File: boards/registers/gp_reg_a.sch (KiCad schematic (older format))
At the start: 28 parts

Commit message: Annotated schematics, assigned footprints
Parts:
- C28, C29: renamed from C?; footprint (none) -> Capacitor_SMD:C_0805_2012Metric
- D54, D55, D56, D57, D58, D59, D60, D61: renamed from D?; footprint (none) -> LED_SMD:LED_0805_2012Metric
- R150, R151, R152, R153, R154, R155, R156, R157, R158, R159, R160, R161, R162, R163, R164, R165: renamed from R?; footprint (none) -> Resistor_SMD:R_0805_2012Metric
- U28: renamed from U?; footprint (none) -> Package_SO:SOIC-20W_7.5x12.8mm_P1.27mm
- U29: renamed from U?; footprint (none) -> Package_SO:SO-20_12.8x7.5mm_P1.27mm

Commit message: PCB attempt
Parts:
- U28: footprint Package_SO:SOIC-20W_7.5x12.8mm_P1.27mm -> Package_SO:TSSOP-20_4.4x6.5mm_P0.65mm
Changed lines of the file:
@@
 AR Path="/5E7CA397/5EA6BD49" Ref="U?"  Part="1"
 AR Path="/5E9FD18D/5EA6BD49" Ref="U29"  Part="1"
-F 0 "U29" H 7600 1150 50  0000 C CNN
+F 0 "U29" H 7650 1150 50  0000 C CNN
 F 1 "74ACT244" H 7550 1050 50  0000 C CNN
 F 2 "Package_SO:SO-20_12.8x7.5mm_P1.27mm" H 7250 1700 50  0001 C CNN
@@
 AR Path="/5E7CA397/5EA6BDD0" Ref="U?"  Part="1"
 AR Path="/5E9FD18D/5EA6BDD0" Ref="U28"  Part="1"
-F 0 "U28" H 5100 1150 50  0000 C CNN
+F 0 "U28" H 5150 1150 50  0000 C CNN
 F 1 "74AC273" H 5100 1050 50  0000 C CNN
-F 2 "Package_SO:SOIC-20W_7.5x12.8mm_P1.27mm" H 4750 1700 50  0001 C CNN
+F 2 "Package_SO:TSSOP-20_4.4x6.5mm_P0.65mm" H 4750 1700 50  0001 C CNN
 F 3 "https://assets.nexperia.com/documents/data-sheet/74HC_HCT273.pdf" H 4750 1700 50  0001 C CNN
 	1    4750 1700

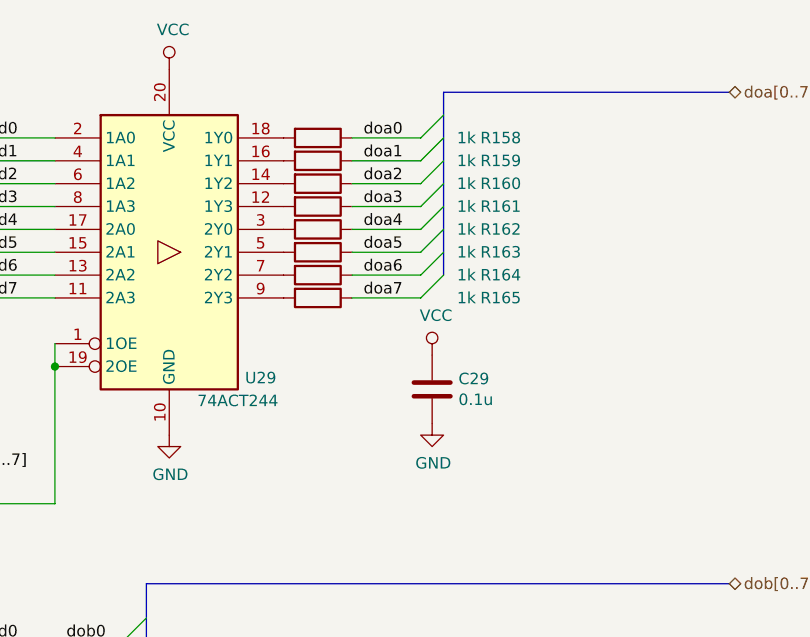
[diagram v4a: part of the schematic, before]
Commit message: CPU registers board
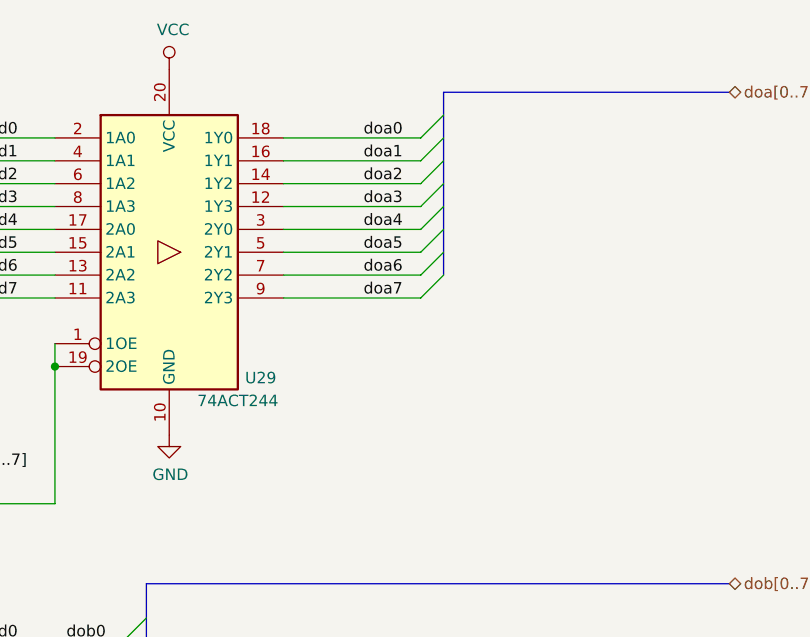
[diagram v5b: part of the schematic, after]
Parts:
- removed C29: 0.1u, Capacitor_SMD:C_0805_2012Metric, symbol Device:C
- removed R158, R159, R160, R161, R162, R163, R164, R165: 1k, Resistor_SMD:R_0805_2012Metric, symbol Device:R
- U29: footprint Package_SO:SO-20_12.8x7.5mm_P1.27mm -> Package_SO:TSSOP-20_4.4x6.5mm_P0.65mm
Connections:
- net doa0: now also U29.18 (1Y0)
- net doa1: now also U29.16 (1Y1)
- net doa2: now also U29.14 (1Y2)
- net doa3: now also U29.12 (1Y3)
- net doa4: now also U29.3 (2Y0)
- net doa5: now also U29.5 (2Y1)
- net doa6: now also U29.7 (2Y2)
- net doa7: now also U29.9 (2Y3)
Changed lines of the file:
@@
 F 0 "U29" H 7650 1150 50  0000 C CNN
 F 1 "74ACT244" H 7550 1050 50  0000 C CNN
-F 2 "Package_SO:SO-20_12.8x7.5mm_P1.27mm" H 7250 1700 50  0001 C CNN
+F 2 "Package_SO:TSSOP-20_4.4x6.5mm_P0.65mm" H 7250 1700 50  0001 C CNN
 F 3 "https://assets.nexperia.com/documents/data-sheet/74HC_HCT244.pdf" H 7250 1700 50  0001 C CNN
 	1    7250 1700
@@
 Entry Wire Line
 	8350 1900 8450 1800
-Wire Wire Line
-	8350 1200 8050 1200
-Wire Wire Line
-	8050 1300 8350 1300
-Wire Wire Line
-	8350 1400 8050 1400
-Wire Wire Line
-	8050 1500 8350 1500
-Wire Wire Line
-	8350 1600 8050 1600
-Wire Wire Line
-	8050 1700 8350 1700
-Wire Wire Line
-	8350 1800 8050 1800
-Wire Wire Line
-	8050 1900 8350 1900
 Text Label 6500 1200 0    50   ~ 0
 d0
@@
 $Comp
 L Device:C C?
-U 1 1 5EA6BED9
-P 8400 2300
-AR Path="/5E73B7F6/5EA6BED9" Ref="C?"  Part="1"
-AR Path="/5E7CA397/5EA6BED9" Ref="C?"  Part="1"
-AR Path="/5E9FD18D/5EA6BED9" Ref="C29"  Part="1"
-F 0 "C29" H 8515 2346 50  0000 L CNN
-F 1 "0.1u" H 8515 2255 50  0000 L CNN
-F 2 "Capacitor_SMD:C_0805_2012Metric" H 8438 2150 50  0001 C CNN
-F 3 "~" H 8400 2300 50  0001 C CNN
-	1    8400 2300
-	1    0    0    -1
-$EndComp
-$Comp
-L power:GND #PWR?
-U 1 1 5EA6BEDF
-P 8400 2450
-AR Path="/5E73B7F6/5EA6BEDF" Ref="#PWR?"  Part="1"
-AR Path="/5E7CA397/5EA6BEDF" Ref="#PWR?"  Part="1"
-AR Path="/5E9FD18D/5EA6BEDF" Ref="#PWR0189"  Part="1"
-F 0 "#PWR0189" H 8400 2200 50  0001 C CNN
-F 1 "GND" H 8405 2277 50  0000 C CNN
-F 2 "" H 8400 2450 50  0001 C CNN
-F 3 "" H 8400 2450 50  0001 C CNN
-	1    8400 2450
-	1    0    0    -1
-$EndComp
-$Comp
-L power:VCC #PWR?
-U 1 1 5EA6BEE5
-P 8400 2150
-AR Path="/5E73B7F6/5EA6BEE5" Ref="#PWR?"  Part="1"
-AR Path="/5E7CA397/5EA6BEE5" Ref="#PWR?"  Part="1"
-AR Path="/5E9FD18D/5EA6BEE5" Ref="#PWR0188"  Part="1"
-F 0 "#PWR0188" H 8400 2000 50  0001 C CNN
-F 1 "VCC" H 8417 2323 50  0000 C CNN
-F 2 "" H 8400 2150 50  0001 C CNN
-F 3 "" H 8400 2150 50  0001 C CNN
-	1    8400 2150
-	1    0    0    -1
-$EndComp
-$Comp
-L Device:C C?
 U 1 1 5EA6BEEB
 P 4050 2400
@@
 	0    1    1    0
 $EndComp
-$Comp
-L Device:R R?
-U 1 1 5EA6BEFD
-P 7900 1200
-AR Path="/5E7CA397/5EA6BEFD" Ref="R?"  Part="1"
-AR Path="/5E73B7F6/5EA6BEFD" Ref="R?"  Part="1"
-AR Path="/5E9FD18D/5EA6BEFD" Ref="R158"  Part="1"
-F 0 "R158" V 7900 2000 50  0000 C CNN
-F 1 "1k" V 7900 1850 50  0000 C CNN
-F 2 "Resistor_SMD:R_0805_2012Metric" V 7830 1200 50  0001 C CNN
-F 3 "~" H 7900 1200 50  0001 C CNN
-	1    7900 1200
-	0    1    1    0
-$EndComp
-$Comp
-L Device:R R?
-U 1 1 5EA6BF03
-P 7900 1300
-AR Path="/5E7CA397/5EA6BF03" Ref="R?"  Part="1"
-AR Path="/5E73B7F6/5EA6BF03" Ref="R?"  Part="1"
-AR Path="/5E9FD18D/5EA6BF03" Ref="R159"  Part="1"
-F 0 "R159" V 7900 2100 50  0000 C CNN
-F 1 "1k" V 7900 1950 50  0000 C CNN
-F 2 "Resistor_SMD:R_0805_2012Metric" V 7830 1300 50  0001 C CNN
-F 3 "~" H 7900 1300 50  0001 C CNN
-	1    7900 1300
-	0    1    1    0
-$EndComp
-$Comp
-L Device:R R?
-U 1 1 5EA6BF09
-P 7900 1400
-AR Path="/5E7CA397/5EA6BF09" Ref="R?"  Part="1"
-AR Path="/5E73B7F6/5EA6BF09" Ref="R?"  Part="1"
-AR Path="/5E9FD18D/5EA6BF09" Ref="R160"  Part="1"
-F 0 "R160" V 7900 2200 50  0000 C CNN
-F 1 "1k" V 7900 2050 50  0000 C CNN
-F 2 "Resistor_SMD:R_0805_2012Metric" V 7830 1400 50  0001 C CNN
-F 3 "~" H 7900 1400 50  0001 C CNN
-	1    7900 1400
-	0    1    1    0
-$EndComp
-$Comp
-L Device:R R?
-U 1 1 5EA6BF0F
-P 7900 1500
-AR Path="/5E7CA397/5EA6BF0F" Ref="R?"  Part="1"
-AR Path="/5E73B7F6/5EA6BF0F" Ref="R?"  Part="1"
-AR Path="/5E9FD18D/5EA6BF0F" Ref="R161"  Part="1"
-F 0 "R161" V 7900 2300 50  0000 C CNN
-F 1 "1k" V 7900 2150 50  0000 C CNN
-F 2 "Resistor_SMD:R_0805_2012Metric" V 7830 1500 50  0001 C CNN
-F 3 "~" H 7900 1500 50  0001 C CNN
-	1    7900 1500
-	0    1    1    0
-$EndComp
-$Comp
-L Device:R R?
-U 1 1 5EA6BF15
-P 7900 1600
-AR Path="/5E7CA397/5EA6BF15" Ref="R?"  Part="1"
-AR Path="/5E73B7F6/5EA6BF15" Ref="R?"  Part="1"
-AR Path="/5E9FD18D/5EA6BF15" Ref="R162"  Part="1"
-F 0 "R162" V 7900 2400 50  0000 C CNN
-F 1 "1k" V 7900 2250 50  0000 C CNN
-F 2 "Resistor_SMD:R_0805_2012Metric" V 7830 1600 50  0001 C CNN
-F 3 "~" H 7900 1600 50  0001 C CNN
-	1    7900 1600
-	0    1    1    0
-$EndComp
-$Comp
-L Device:R R?
-U 1 1 5EA6BF1B
-P 7900 1700
-AR Path="/5E7CA397/5EA6BF1B" Ref="R?"  Part="1"
-AR Path="/5E73B7F6/5EA6BF1B" Ref="R?"  Part="1"
-AR Path="/5E9FD18D/5EA6BF1B" Ref="R163"  Part="1"
-F 0 "R163" V 7900 2500 50  0000 C CNN
-F 1 "1k" V 7900 2350 50  0000 C CNN
-F 2 "Resistor_SMD:R_0805_2012Metric" V 7830 1700 50  0001 C CNN
-F 3 "~" H 7900 1700 50  0001 C CNN
-	1    7900 1700
-	0    1    1    0
-$EndComp
-$Comp
-L Device:R R?
-U 1 1 5EA6BF21
-P 7900 1800
-AR Path="/5E7CA397/5EA6BF21" Ref="R?"  Part="1"
-AR Path="/5E73B7F6/5EA6BF21" Ref="R?"  Part="1"
-AR Path="/5E9FD18D/5EA6BF21" Ref="R164"  Part="1"
-F 0 "R164" V 7900 2600 50  0000 C CNN
-F 1 "1k" V 7900 2450 50  0000 C CNN
-F 2 "Resistor_SMD:R_0805_2012Metric" V 7830 1800 50  0001 C CNN
-F 3 "~" H 7900 1800 50  0001 C CNN
-	1    7900 1800
-	0    1    1    0
-$EndComp
-$Comp
-L Device:R R?
-U 1 1 5EA6BF27
-P 7900 1900
-AR Path="/5E7CA397/5EA6BF27" Ref="R?"  Part="1"
-AR Path="/5E73B7F6/5EA6BF27" Ref="R?"  Part="1"
-AR Path="/5E9FD18D/5EA6BF27" Ref="R165"  Part="1"
-F 0 "R165" V 7900 2700 50  0000 C CNN
-F 1 "1k" V 7900 2550 50  0000 C CNN
-F 2 "Resistor_SMD:R_0805_2012Metric" V 7830 1900 50  0001 C CNN
-F 3 "~" H 7900 1900 50  0001 C CNN
-	1    7900 1900
-	0    1    1    0
-$EndComp
 Text HLabel 1650 2800 0    50   Input ~ 0
 ~oea
@@
 Wire Bus Line
 	9700 3150 7150 3150
+Wire Wire Line
+	7750 1900 8350 1900
+Wire Wire Line
+	7750 1800 8350 1800
+Wire Wire Line
+	7750 1700 8350 1700
+Wire Wire Line
+	7750 1600 8350 1600
+Wire Wire Line
+	7750 1500 8350 1500
+Wire Wire Line
+	7750 1400 8350 1400
+Wire Wire Line
+	7750 1300 8350 1300
+Wire Wire Line
+	7750 1200 8350 1200
 Wire Bus Line
 	7150 3150 7150 4000

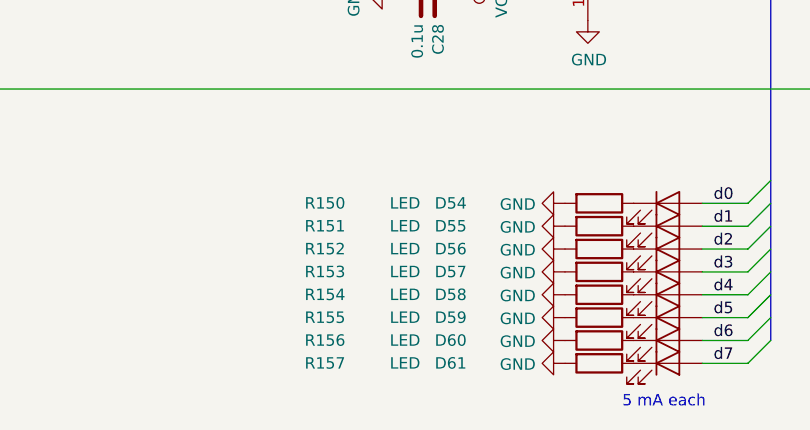
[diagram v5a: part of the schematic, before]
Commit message: LEDs and LED resistors
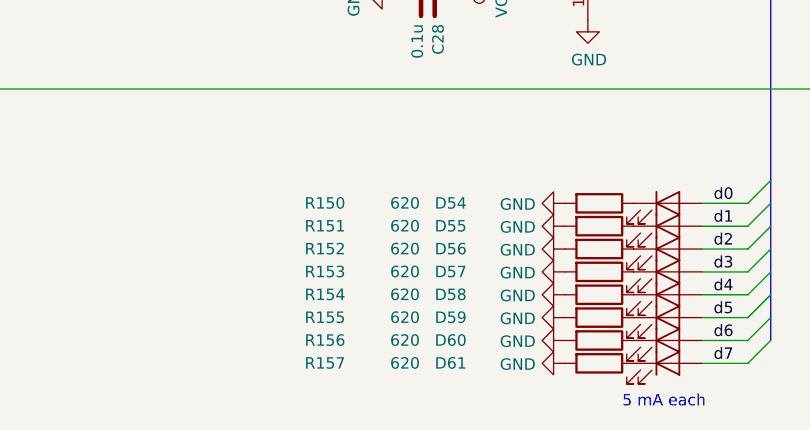
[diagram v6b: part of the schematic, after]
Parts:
- D54, D55, D56, D57, D58, D59, D60, D61: value LED -> KP-2012EC
- R150, R151, R152, R153, R154, R155, R156, R157: value LED -> 620
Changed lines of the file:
@@
 AR Path="/5E9FD18D/5EA6BE13" Ref="D54"  Part="1"
 F 0 "D54" H 4150 3300 50  0000 C CNN
-F 1 "LED" H 5093 3425 50  0001 C CNN
+F 1 "KP-2012EC" H 5093 3425 50  0001 C CNN
 F 2 "LED_SMD:LED_0805_2012Metric" H 5100 3300 50  0001 C CNN
 F 3 "~" H 5100 3300 50  0001 C CNN
@@
 AR Path="/5E9FD18D/5EA6BE19" Ref="R150"  Part="1"
 F 0 "R150" V 4800 2100 50  0000 C CNN
-F 1 "LED" V 4800 2450 50  0000 C CNN
+F 1 "620" V 4800 2450 50  0000 C CNN
 F 2 "Resistor_SMD:R_0805_2012Metric" V 4730 3300 50  0001 C CNN
 F 3 "~" H 4800 3300 50  0001 C CNN
@@
 AR Path="/5E9FD18D/5EA6BE25" Ref="D55"  Part="1"
 F 0 "D55" H 4150 3400 50  0000 C CNN
-F 1 "LED" H 5093 3525 50  0001 C CNN
+F 1 "KP-2012EC" H 5093 3525 50  0001 C CNN
 F 2 "LED_SMD:LED_0805_2012Metric" H 5100 3400 50  0001 C CNN
 F 3 "~" H 5100 3400 50  0001 C CNN
@@
 AR Path="/5E9FD18D/5EA6BE2B" Ref="R151"  Part="1"
 F 0 "R151" V 4800 2200 50  0000 C CNN
-F 1 "LED" V 4800 2550 50  0000 C CNN
+F 1 "620" V 4800 2550 50  0000 C CNN
 F 2 "Resistor_SMD:R_0805_2012Metric" V 4730 3400 50  0001 C CNN
 F 3 "~" H 4800 3400 50  0001 C CNN
@@
 AR Path="/5E9FD18D/5EA6BE37" Ref="D56"  Part="1"
 F 0 "D56" H 4150 3500 50  0000 C CNN
-F 1 "LED" H 5093 3625 50  0001 C CNN
+F 1 "KP-2012EC" H 5093 3625 50  0001 C CNN
 F 2 "LED_SMD:LED_0805_2012Metric" H 5100 3500 50  0001 C CNN
 F 3 "~" H 5100 3500 50  0001 C CNN
@@
 AR Path="/5E9FD18D/5EA6BE3D" Ref="R152"  Part="1"
 F 0 "R152" V 4800 2300 50  0000 C CNN
-F 1 "LED" V 4800 2650 50  0000 C CNN
+F 1 "620" V 4800 2650 50  0000 C CNN
 F 2 "Resistor_SMD:R_0805_2012Metric" V 4730 3500 50  0001 C CNN
 F 3 "~" H 4800 3500 50  0001 C CNN
@@
 AR Path="/5E9FD18D/5EA6BE49" Ref="D57"  Part="1"
 F 0 "D57" H 4150 3600 50  0000 C CNN
-F 1 "LED" H 5093 3725 50  0001 C CNN
+F 1 "KP-2012EC" H 5093 3725 50  0001 C CNN
 F 2 "LED_SMD:LED_0805_2012Metric" H 5100 3600 50  0001 C CNN
 F 3 "~" H 5100 3600 50  0001 C CNN
@@
 AR Path="/5E9FD18D/5EA6BE4F" Ref="R153"  Part="1"
 F 0 "R153" V 4800 2400 50  0000 C CNN
-F 1 "LED" V 4800 2750 50  0000 C CNN
+F 1 "620" V 4800 2750 50  0000 C CNN
 F 2 "Resistor_SMD:R_0805_2012Metric" V 4730 3600 50  0001 C CNN
 F 3 "~" H 4800 3600 50  0001 C CNN
@@
 AR Path="/5E9FD18D/5EA6BE5B" Ref="D58"  Part="1"
 F 0 "D58" H 4150 3700 50  0000 C CNN
-F 1 "LED" H 5093 3825 50  0001 C CNN
+F 1 "KP-2012EC" H 5093 3825 50  0001 C CNN
 F 2 "LED_SMD:LED_0805_2012Metric" H 5100 3700 50  0001 C CNN
 F 3 "~" H 5100 3700 50  0001 C CNN
@@
 AR Path="/5E9FD18D/5EA6BE61" Ref="R154"  Part="1"
 F 0 "R154" V 4800 2500 50  0000 C CNN
-F 1 "LED" V 4800 2850 50  0000 C CNN
+F 1 "620" V 4800 2850 50  0000 C CNN
 F 2 "Resistor_SMD:R_0805_2012Metric" V 4730 3700 50  0001 C CNN
 F 3 "~" H 4800 3700 50  0001 C CNN
@@
 AR Path="/5E9FD18D/5EA6BE6D" Ref="D59"  Part="1"
 F 0 "D59" H 4150 3800 50  0000 C CNN
-F 1 "LED" H 5093 3925 50  0001 C CNN
+F 1 "KP-2012EC" H 5093 3925 50  0001 C CNN
 F 2 "LED_SMD:LED_0805_2012Metric" H 5100 3800 50  0001 C CNN
 F 3 "~" H 5100 3800 50  0001 C CNN
@@
 AR Path="/5E9FD18D/5EA6BE73" Ref="R155"  Part="1"
 F 0 "R155" V 4800 2600 50  0000 C CNN
-F 1 "LED" V 4800 2950 50  0000 C CNN
+F 1 "620" V 4800 2950 50  0000 C CNN
 F 2 "Resistor_SMD:R_0805_2012Metric" V 4730 3800 50  0001 C CNN
 F 3 "~" H 4800 3800 50  0001 C CNN
@@
 AR Path="/5E9FD18D/5EA6BE7F" Ref="D60"  Part="1"
 F 0 "D60" H 4150 3900 50  0000 C CNN
-F 1 "LED" H 5093 4025 50  0001 C CNN
+F 1 "KP-2012EC" H 5093 4025 50  0001 C CNN
 F 2 "LED_SMD:LED_0805_2012Metric" H 5100 3900 50  0001 C CNN
 F 3 "~" H 5100 3900 50  0001 C CNN
@@
 AR Path="/5E9FD18D/5EA6BE85" Ref="R156"  Part="1"
 F 0 "R156" V 4800 2700 50  0000 C CNN
-F 1 "LED" V 4800 3050 50  0000 C CNN
+F 1 "620" V 4800 3050 50  0000 C CNN
 F 2 "Resistor_SMD:R_0805_2012Metric" V 4730 3900 50  0001 C CNN
 F 3 "~" H 4800 3900 50  0001 C CNN
@@
 AR Path="/5E9FD18D/5EA6BE91" Ref="D61"  Part="1"
 F 0 "D61" H 4150 4000 50  0000 C CNN
-F 1 "LED" H 5093 4125 50  0001 C CNN
+F 1 "KP-2012EC" H 5093 4125 50  0001 C CNN
 F 2 "LED_SMD:LED_0805_2012Metric" H 5100 4000 50  0001 C CNN
 F 3 "~" H 5100 4000 50  0001 C CNN
@@
 AR Path="/5E9FD18D/5EA6BE97" Ref="R157"  Part="1"
 F 0 "R157" V 4800 2800 50  0000 C CNN
-F 1 "LED" V 4800 3150 50  0000 C CNN
+F 1 "620" V 4800 3150 50  0000 C CNN
 F 2 "Resistor_SMD:R_0805_2012Metric" V 4730 4000 50  0001 C CNN
 F 3 "~" H 4800 4000 50  0001 C CNN

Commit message: Part names
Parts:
- U28: value 74AC273 -> MC74AC273DTR2G
- U29: value 74ACT244 -> SN74ACT244PW
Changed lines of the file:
@@
 AR Path="/5E9FD18D/5EA6BD49" Ref="U29"  Part="1"
 F 0 "U29" H 7650 1150 50  0000 C CNN
-F 1 "74ACT244" H 7550 1050 50  0000 C CNN
+F 1 "SN74ACT244PW" H 7550 1050 50  0000 C CNN
 F 2 "Package_SO:TSSOP-20_4.4x6.5mm_P0.65mm" H 7250 1700 50  0001 C CNN
 F 3 "https://assets.nexperia.com/documents/data-sheet/74HC_HCT244.pdf" H 7250 1700 50  0001 C CNN
@@
 AR Path="/5E9FD18D/5EA6BDD0" Ref="U28"  Part="1"
 F 0 "U28" H 5150 1150 50  0000 C CNN
-F 1 "74AC273" H 5100 1050 50  0000 C CNN
+F 1 "MC74AC273DTR2G" H 5100 1050 50  0000 C CNN
 F 2 "Package_SO:TSSOP-20_4.4x6.5mm_P0.65mm" H 4750 1700 50  0001 C CNN
 F 3 "https://assets.nexperia.com/documents/data-sheet/74HC_HCT273.pdf" H 4750 1700 50  0001 C CNN
